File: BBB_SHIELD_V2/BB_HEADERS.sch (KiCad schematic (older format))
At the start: 10 parts, among them J4 P8, J5 P9, SW1 SW_Push, SW2 SW_Push, U4 CD74HCx4066, U5 CD74HCx4066

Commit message: Changed to high-side switching of power supply to boards.  Changed footprints to SOIC.  Misc other changes.
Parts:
- removed TP11, TP12: TestPoint_2Pole, Connector_PinHeader_1.27mm:PinHeader_1x02_P1.27mm_Vertical, symbol Connector:TestPoint_2Pole
- added TPSCL1, TPSDA1: TestPoint, Connector_PinHeader_1.27mm:PinHeader_1x01_P1.27mm_Vertical, symbol Connector:TestPoint
- P1: renamed from J4; value P8 -> BBCONN; DKPN (none) -> A26529-23-ND; NOTES (none) -> VER 2019-11-25
- P2: renamed from J5; value P9 -> BBCONN; DKPN (none) -> A26529-23-ND; NOTES (none) -> VER 2019-11-25
- R18: renamed from R21; value 5K -> 5K6; DKPN (none) -> 311-5.60KCRCT-ND; MFG (none) -> YAGEO; MFGPN (none) -> RC0805FR-075K6L; NOTES (none) -> CT, VER 2018-12-09
- R19: renamed from R22; value 5K -> 5K6; DKPN (none) -> 311-5.60KCRCT-ND; MFG (none) -> YAGEO; MFGPN (none) -> RC0805FR-075K6L; NOTES (none) -> CT, VER 2018-12-09
- SW1, SW2: NOTES (none) -> BULK, VER 2018-11-25
- U2: renamed from U4; footprint Package_SO:TSSOP-14_4.4x5mm_P0.65mm -> Package_SO:SOIC-14_3.9x8.7mm_P1.27mm; DKPN (none) -> 296-16703-1-ND; MFGPN (none) -> CD74HC4066PWR; NOTES (none) -> BULK, VER 2018-11-25
- U3: renamed from U5; footprint Package_SO:TSSOP-14_4.4x5mm_P0.65mm -> Package_SO:SOIC-14_3.9x8.7mm_P1.27mm; DKPN (none) -> 296-16703-1-ND; MFGPN (none) -> CD74HC4066PWR; NOTES (none) -> BULK, VER 2018-11-25
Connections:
- wire segments 81 -> 82
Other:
- note added: "AUX_1 -- P9_27\nAUX_2 -- P8_39\nENABLE -- P8_40\n"
- moved on the sheet: P1

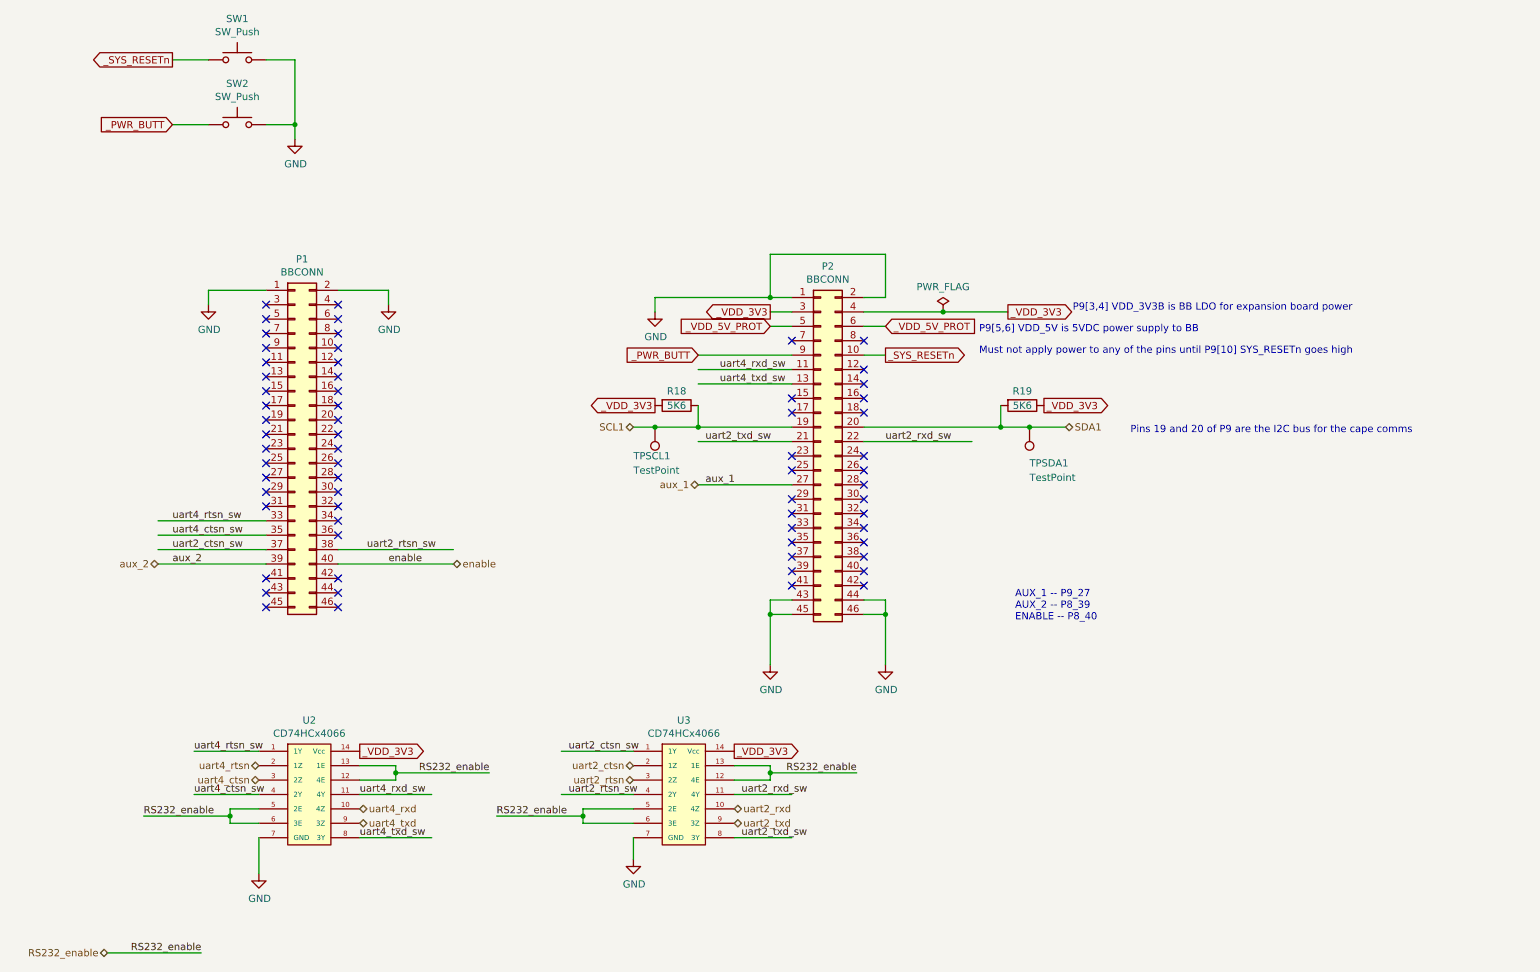
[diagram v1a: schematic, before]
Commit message: Cleaned up schematic.
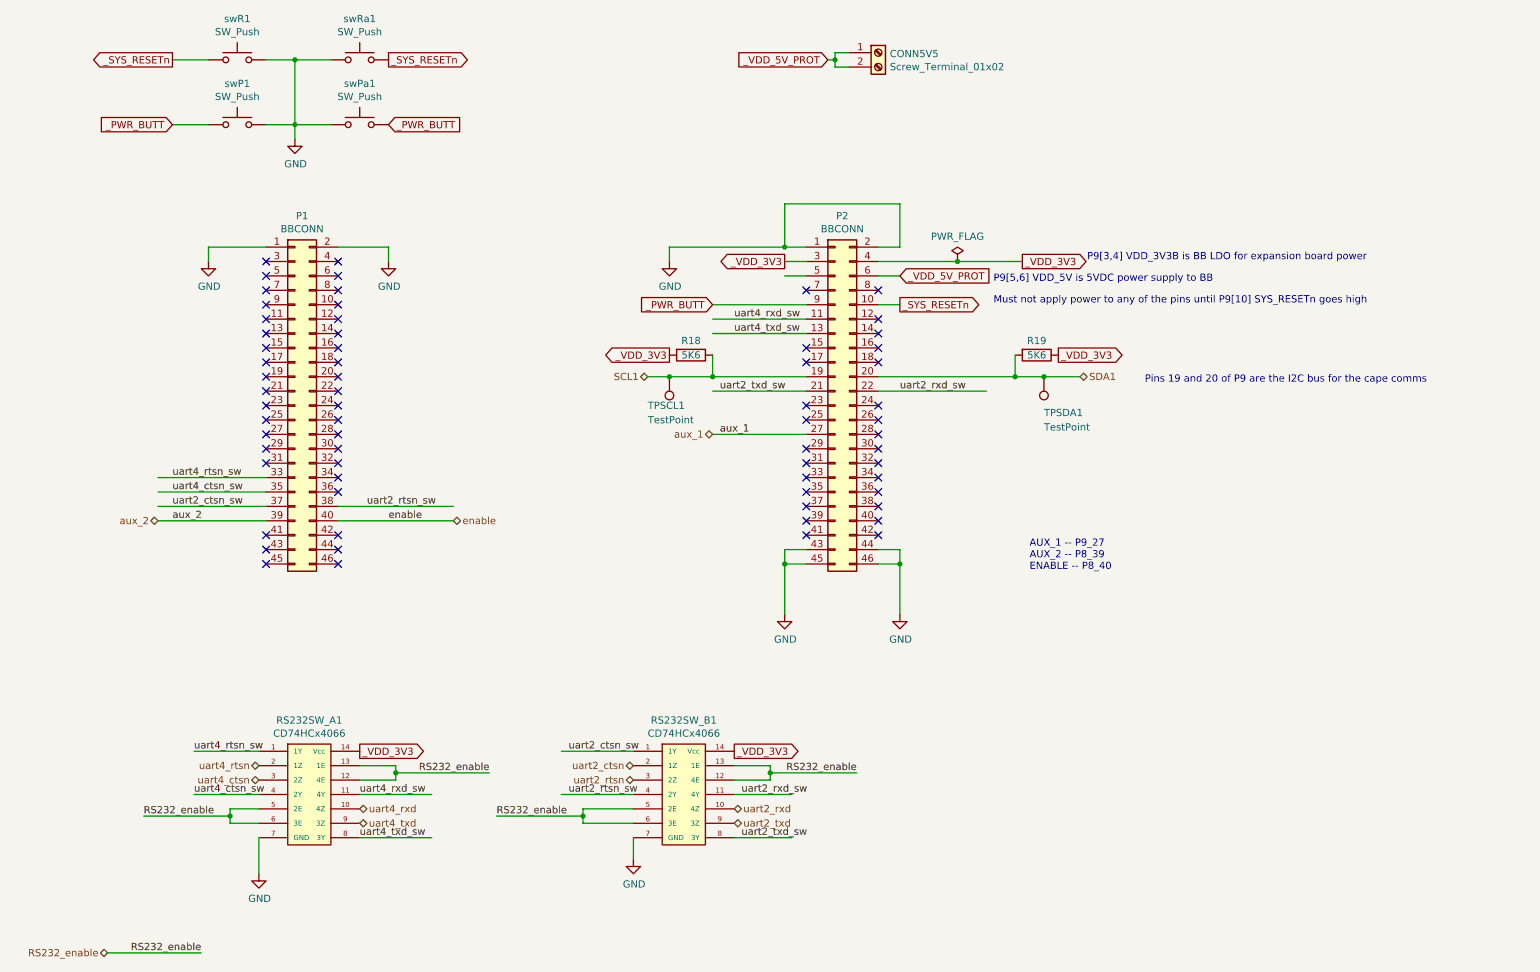
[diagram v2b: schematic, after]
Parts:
- added CONN5V5: Screw_Terminal_01x02, CUSTOM_FOOTPRINTS:OSTTA024163, symbol Connector:Screw_Terminal_01x02
- added swPa1, swRa1: SW_Push, CUSTOM_FOOTPRINTS:KSC3_6.20x6.20_J-LEAD, symbol Switch:SW_Push
- RS232SW_A1: renamed from U2; DKPN 296-16703-1-ND -> 296-9224-1-ND; MFGPN CD74HC4066PWR -> CD74HC4066M96
- RS232SW_B1: renamed from U3; DKPN 296-16703-1-ND -> 296-9224-1-ND; MFGPN CD74HC4066PWR -> CD74HC4066M96
- renumbered SW2 to swP1, SW1 to swR1
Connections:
- wire segments 82 -> 89
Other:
- moved on the sheet: P1, P2, R18, R19, TPSCL1, TPSDA1

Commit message: Schematic cleanup and refinement.
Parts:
- removed swPa1, swRa1: SW_Push, CUSTOM_FOOTPRINTS:KSC3_6.20x6.20_J-LEAD, symbol Switch:SW_Push
- renumbered P1 to P8, P2 to P9
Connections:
- wire segments 89 -> 87
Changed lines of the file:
@@
 $EndDescr
 $Comp
-L Connector_Generic:Conn_02x23_Odd_Even P1
+L Connector_Generic:Conn_02x23_Odd_Even P8
 U 1 1 5B9EA682
 P 2650 3650
-F 0 "P1" H 2700 4967 50  0000 C CNN
+F 0 "P8" H 2700 4967 50  0000 C CNN
 F 1 "BBCONN" H 2700 4876 50  0000 C CNN
 F 2 "Connector_PinHeader_2.54mm:PinHeader_2x23_P2.54mm_Vertical" H 2650 3650 50  0001 C CNN
@@
 	2050 2550 2450 2550
 $Comp
-L Connector_Generic:Conn_02x23_Odd_Even P2
+L Connector_Generic:Conn_02x23_Odd_Even P9
 U 1 1 5B9EA71F
 P 6400 3650
-F 0 "P2" H 6450 4967 50  0000 C CNN
+F 0 "P9" H 6450 4967 50  0000 C CNN
 F 1 "BBCONN" H 6450 4876 50  0000 C CNN
 F 2 "Connector_PinHeader_2.54mm:PinHeader_2x23_P2.54mm_Vertical" H 6400 3650 50  0001 C CNN
@@
 	6400 1300 6500 1300
 Connection ~ 6400 1250
-$Comp
-L Switch:SW_Push swRa1
-U 1 1 5D130323
-P 3100 1250
-F 0 "swRa1" H 3100 1535 50  0000 C CNN
-F 1 "SW_Push" H 3100 1444 50  0000 C CNN
-F 2 "CUSTOM_FOOTPRINTS:KSC3_6.20x6.20_J-LEAD" H 3100 1450 50  0001 C CNN
-F 3 "" H 3100 1450 50  0001 C CNN
-F 4 "BULK, VER 2018-11-25" H 850 0   50  0001 C CNN "NOTES"
-F 5 "CKN12186CT-ND" H 3100 1250 50  0001 C CNN "DKPN"
-F 6 "KSC441J DCT 70SH LFS" H 3100 1250 50  0001 C CNN "MFGPN"
-	1    3100 1250
-	1    0    0    -1
-$EndComp
-Connection ~ 2650 1250
-Wire Wire Line
-	2650 1250 2900 1250
-Wire Wire Line
-	2650 1700 2900 1700
-Text GLabel 3300 1250 2    50   Output ~ 0
-_SYS_RESETn
-Text GLabel 3300 1700 2    50   Input ~ 0
-_PWR_BUTT
-$Comp
-L Switch:SW_Push swPa1
-U 1 1 5D13AF83
-P 3100 1700
-F 0 "swPa1" H 3100 1985 50  0000 C CNN
-F 1 "SW_Push" H 3100 1894 50  0000 C CNN
-F 2 "CUSTOM_FOOTPRINTS:KSC3_6.20x6.20_J-LEAD" H 3100 1900 50  0001 C CNN
-F 3 "" H 3100 1900 50  0001 C CNN
-F 4 "BULK, VER 2018-11-25" H 850 450 50  0001 C CNN "NOTES"
-F 5 "CKN12186CT-ND" H 3100 1700 50  0001 C CNN "DKPN"
-F 6 "KSC441J DCT 70SH LFS" H 3100 1700 50  0001 C CNN "MFGPN"
-	1    3100 1700
-	1    0    0    -1
-$EndComp
+Text GLabel 6050 2750 0    50   Input ~ 0
+_VDD_5V_PROT
 $EndSCHEMATC

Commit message: Rev 2 problem fixes.
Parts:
- CONN5V5: NOTES (none) -> VER,2019-07-16,BULK
- P8, P9: NOTES VER 2019-11-25 -> VER,2019-07-16,BULK
- R18, R19: value 5K6 -> 4K7; DKPN 311-5.60KCRCT-ND -> 541-4131-1-ND; MFG YAGEO -> VISHAY; MFGPN RC0805FR-075K6L -> CRCW08054K70FKEAC; NOTES CT, VER 2018-12-09 -> VER,2019-07-17,CT
- RS232SW_A1, RS232SW_B1: MFG (none) -> TEXAS INSTRUMENTS; NOTES BULK, VER 2018-11-25 -> VER,2019-07-15,CT
- swP1, swR1: NOTES BULK, VER 2018-11-25 -> VER,2019-07-16,CT
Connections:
- wire segments 87 -> 84
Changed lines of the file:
@@
 F 3 "" H 2650 3650 50  0001 C CNN
 F 4 "A26529-23-ND" H -1150 -300 50  0001 C CNN "DKPN"
-F 5 "VER 2019-11-25" H -1150 -300 50  0001 C CNN "NOTES"
+F 5 "VER,2019-07-16,BULK" H -1150 -300 50  0001 C CNN "NOTES"
 	1    2650 3650
 	1    0    0    -1
@@
 Wire Wire Line
 	7250 2650 7700 2650
-Text GLabel 6350 1250 0    50   Input ~ 0
+Text GLabel 6400 1200 0    50   BiDi ~ 0
 _VDD_5V_PROT
 Text GLabel 6850 2750 2    50   Input ~ 0
@@
 Text Notes 7500 2800 0    50   ~ 0
 P9[5,6] VDD_5V is 5VDC power supply to BB
-Text GLabel 6850 2950 2    50   Output ~ 0
+Text GLabel 6850 2950 2    50   BiDi ~ 0
 _SYS_RESETn
 Text Notes 7500 2950 0    50   ~ 0
@@
 F 3 "" H 6400 3650 50  0001 C CNN
 F 4 "A26529-23-ND" H 100 -350 50  0001 C CNN "DKPN"
-F 5 "VER 2019-11-25" H 100 -350 50  0001 C CNN "NOTES"
+F 5 "VER,2019-07-16,BULK" H 100 -350 50  0001 C CNN "NOTES"
 	1    6400 3650
 	1    0    0    -1
@@
 Text Label 3150 4350 0    50   ~ 0
 uart2_rtsn_sw
-Text GLabel 5550 2950 0    50   Input ~ 0
+Text GLabel 5550 2950 0    50   BiDi ~ 0
 _PWR_BUTT
 Wire Wire Line
@@
 Text Label 3300 4450 0    50   ~ 0
 enable
-Text GLabel 1800 1700 0    50   Input ~ 0
+Text GLabel 1800 1700 0    50   BiDi ~ 0
 _PWR_BUTT
-Text GLabel 1800 1250 0    50   Output ~ 0
+Text GLabel 1800 1250 0    50   BiDi ~ 0
 _SYS_RESETn
 $Comp
@@
 F 2 "Button_Switch_THT:SW_PUSH_6mm" H 2250 1900 50  0001 C CNN
 F 3 "" H 2250 1900 50  0001 C CNN
-F 4 "BULK, VER 2018-11-25" H 0   0   50  0001 C CNN "NOTES"
+F 4 "VER,2019-07-16,CT" H 0   0   50  0001 C CNN "NOTES"
 	1    2250 1700
 	1    0    0    -1
@@
 F 2 "Button_Switch_THT:SW_PUSH_6mm" H 2250 1450 50  0001 C CNN
 F 3 "" H 2250 1450 50  0001 C CNN
-F 4 "BULK, VER 2018-11-25" H 0   0   50  0001 C CNN "NOTES"
+F 4 "VER,2019-07-16,CT" H 0   0   50  0001 C CNN "NOTES"
 	1    2250 1250
 	1    0    0    -1
@@
 F 4 "296-9224-1-ND" H 0   0   50  0001 C CNN "DKPN"
 F 5 "CD74HC4066M96" H 0   0   50  0001 C CNN "MFGPN"
-F 6 "BULK, VER 2018-11-25" H 0   0   50  0001 C CNN "NOTES"
+F 6 "VER,2019-07-15,CT" H 0   0   50  0001 C CNN "NOTES"
+F 7 "TEXAS INSTRUMENTS" H 0   0   50  0001 C CNN "MFG"
 	1    2750 6250
 	1    0    0    -1
@@
 F 4 "296-9224-1-ND" H 0   0   50  0001 C CNN "DKPN"
 F 5 "CD74HC4066M96" H 0   0   50  0001 C CNN "MFGPN"
-F 6 "BULK, VER 2018-11-25" H 0   0   50  0001 C CNN "NOTES"
+F 6 "VER,2019-07-15,CT" H 0   0   50  0001 C CNN "NOTES"
+F 7 "TEXAS INSTRUMENTS" H 0   0   50  0001 C CNN "MFG"
 	1    5350 6250
 	1    0    0    -1
@@
 P 5400 3300
 F 0 "R18" V 5300 3300 50  0000 C CNN
-F 1 "5K6" V 5400 3300 50  0000 C CNN
+F 1 "4K7" V 5400 3300 50  0000 C CNN
 F 2 "Resistor_SMD:R_0805_2012Metric" V 5330 3300 50  0001 C CNN
 F 3 "" H 5400 3300 50  0001 C CNN
-F 4 "CT, VER 2018-12-09" H 100 -350 50  0001 C CNN "NOTES"
-F 5 "311-5.60KCRCT-ND" H 100 -350 50  0001 C CNN "DKPN"
-F 6 "YAGEO" H 100 -350 50  0001 C CNN "MFG"
-F 7 "RC0805FR-075K6L" H 100 -350 50  0001 C CNN "MFGPN"
+F 4 "VER,2019-07-17,CT" H 100 -350 50  0001 C CNN "NOTES"
+F 5 "541-4131-1-ND" H 100 -350 50  0001 C CNN "DKPN"
+F 6 "VISHAY" H 100 -350 50  0001 C CNN "MFG"
+F 7 "CRCW08054K70FKEAC" H 100 -350 50  0001 C CNN "MFGPN"
 	1    5400 3300
 	0    1    1    0
@@
 P 7800 3300
 F 0 "R19" V 7700 3300 50  0000 C CNN
-F 1 "5K6" V 7800 3300 50  0000 C CNN
+F 1 "4K7" V 7800 3300 50  0000 C CNN
 F 2 "Resistor_SMD:R_0805_2012Metric" V 7730 3300 50  0001 C CNN
 F 3 "" H 7800 3300 50  0001 C CNN
-F 4 "CT, VER 2018-12-09" H 100 -350 50  0001 C CNN "NOTES"
-F 5 "311-5.60KCRCT-ND" H 100 -350 50  0001 C CNN "DKPN"
-F 6 "YAGEO" H 100 -350 50  0001 C CNN "MFG"
-F 7 "RC0805FR-075K6L" H 100 -350 50  0001 C CNN "MFGPN"
+F 4 "VER,2019-07-17,CT" H 100 -350 50  0001 C CNN "NOTES"
+F 5 "541-4131-1-ND" H 100 -350 50  0001 C CNN "DKPN"
+F 6 "VISHAY" H 100 -350 50  0001 C CNN "MFG"
+F 7 "CRCW08054K70FKEAC" H 100 -350 50  0001 C CNN "MFGPN"
 	1    7800 3300
 	0    1    1    0
@@
 F 2 "CUSTOM_FOOTPRINTS:OSTTA024163" H 6700 1200 50  0001 C CNN
 F 3 "~" H 6700 1200 50  0001 C CNN
+F 4 "VER,2019-07-16,BULK" H 0   0   50  0001 C CNN "NOTES"
 	1    6700 1200
 	1    0    0    -1
@@
 	6500 1200 6400 1200
 Wire Wire Line
-	6400 1200 6400 1250
-Wire Wire Line
-	6400 1250 6350 1250
-Wire Wire Line
-	6400 1250 6400 1300
-Wire Wire Line
 	6400 1300 6500 1300
-Connection ~ 6400 1250
 Text GLabel 6050 2750 0    50   Input ~ 0
 _VDD_5V_PROT
+Text GLabel 6400 1300 0    50   BiDi ~ 0
+_VDD_3V3
 $EndSCHEMATC
